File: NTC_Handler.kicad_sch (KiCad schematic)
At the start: 48 parts, among them U11 LMV7239M5/NOPB, U2 LM1117GS-5.0, U3 LM1117GS-5.0, U4 LMV7239M5/NOPB, U5 ADuM1200AR, U6 ADuM1200AR, U7 LM1117GS-5.0, U8 LMV7239M5/NOPB, U9 ADuM1200AR

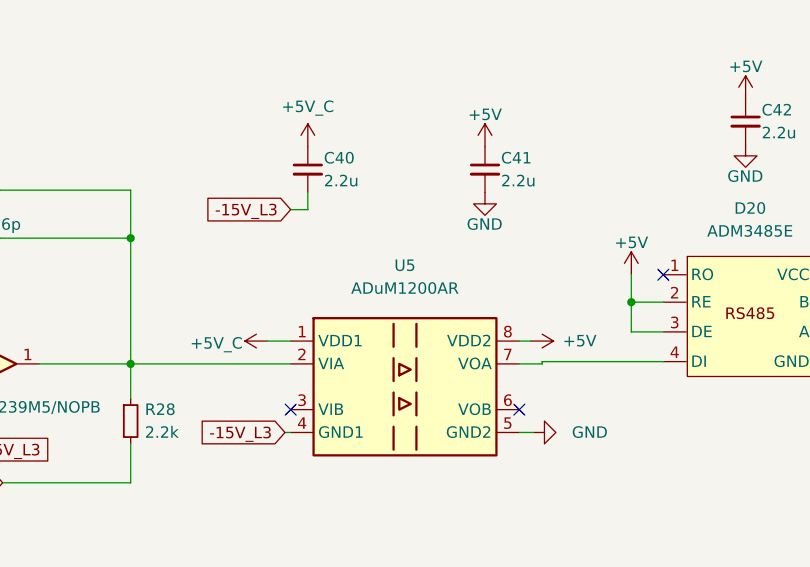
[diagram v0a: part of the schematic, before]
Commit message: Отправил на проверку в резонит: изменил BOM
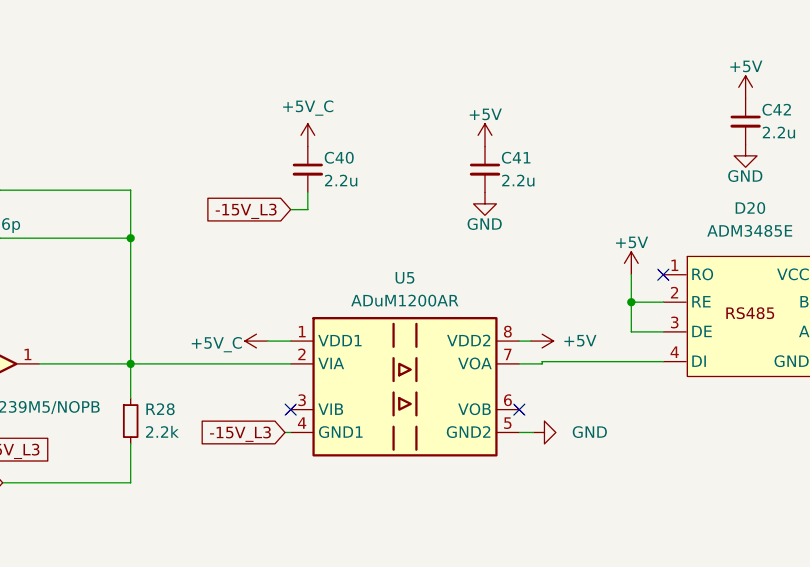
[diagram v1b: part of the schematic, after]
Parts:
- U5, U6, U9: Аналог (none) -> SCM3728ASA
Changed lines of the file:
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@@
 			)
 		)
+		(property "Аналог" "SCM3728ASA"
+			(at 212.725 152.4 0)
+			(effects
+				(font
+					(size 1.27 1.27)
+				)
+				(hide yes)
+			)
+		)
 		(pin "1"
 		)
@@
 			)
 		)
+		(property "Аналог" "SCM3728ASA"
+			(at 212.725 229.235 0)
+			(effects
+				(font
+					(size 1.27 1.27)
+				)
+				(hide yes)
+			)
+		)
 		(pin "1"
 		)
@@
 		(fields_autoplaced yes)
 		(property "Reference" "U5"
-			(at 212.725 63.373 0)
+			(at 212.725 64.77 0)
 			(effects
 				(font
@@
 		)
 		(property "Value" "ADuM1200AR"
-			(at 212.725 65.913 0)
+			(at 212.725 67.31 0)
 			(effects
 				(font
@@
 			(at 212.725 76.835 0)
 			(effects
+				(font
+					(size 1.27 1.27)
+				)
+				(hide yes)
+			)
+		)
+		(property "Аналог" "SCM3728ASA"
+			(at 212.725 76.835 0)
+			(effects

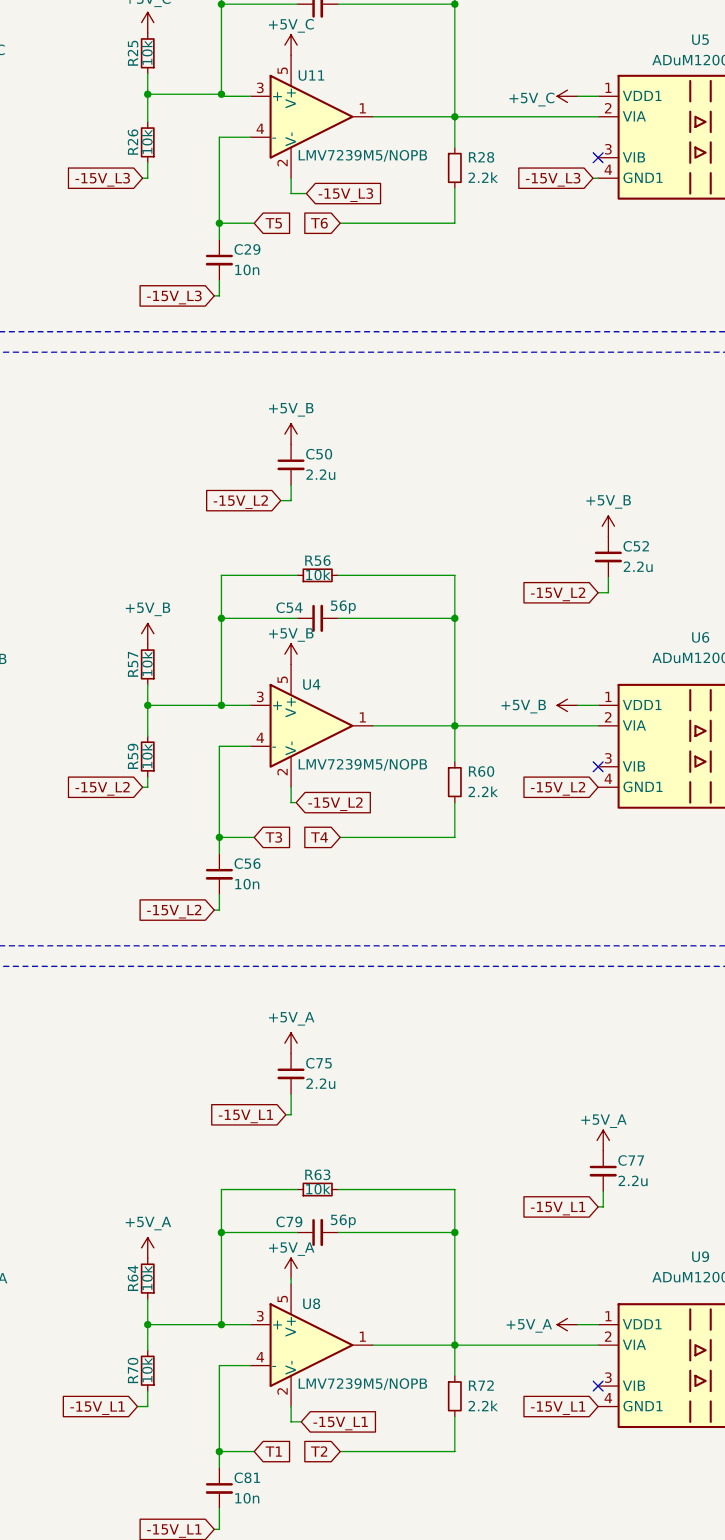
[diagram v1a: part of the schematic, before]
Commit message: Изменения: обновил BOM и названия в схеме
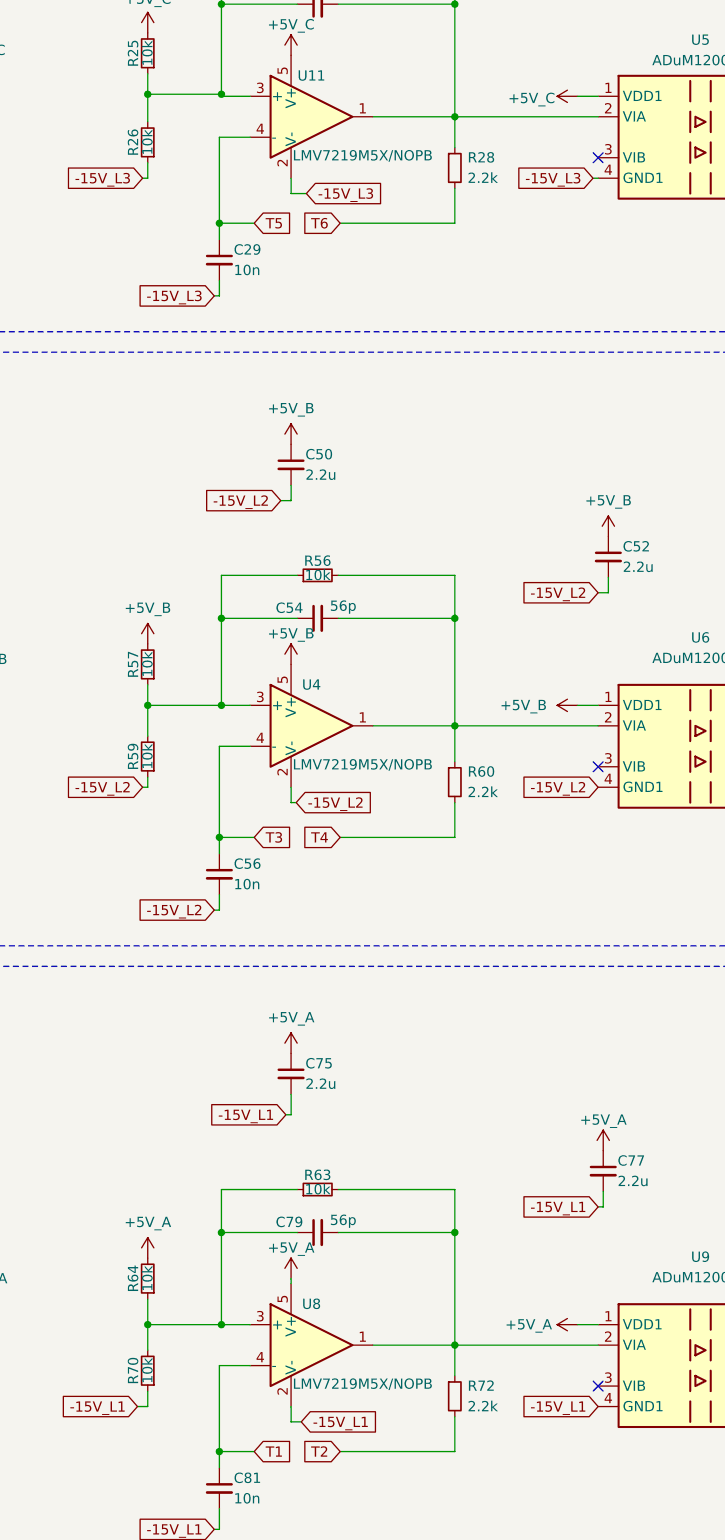
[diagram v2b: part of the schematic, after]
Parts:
- U11, U4, U8: value LMV7239M5/NOPB -> LMV7219M5X/NOPB
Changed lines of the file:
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@@
 			)
 		)
-		(property "Value" "LMV7239M5/NOPB"
+		(property "Value" "LMV7219M5X/NOPB"
 			(at 170.815 154.686 0)
 			(effects
@@
 			)
 		)
-		(property "Value" "LMV7239M5/NOPB"
+		(property "Value" "LMV7219M5X/NOPB"
 			(at 170.815 231.521 0)
 			(effects
@@
 			)
 		)
-		(property "Value" "LMV7239M5/NOPB"
+		(property "Value" "LMV7219M5X/NOPB"
 			(at 170.815 79.121 0)
 			(effects

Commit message: VER2.0: отпаравил файлы в китай, обновил BOM
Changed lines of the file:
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@@
 		)
 		(property "Value" "LMV7219M5X/NOPB"
-			(at 170.815 154.686 0)
+			(at 171.45 154.94 0)
 			(effects
 				(font
@@
 		)
 		(property "Value" "LMV7219M5X/NOPB"
-			(at 170.815 231.521 0)
+			(at 171.45 231.775 0)
 			(effects
 				(font
@@
 		)
 		(property "Value" "LMV7219M5X/NOPB"
-			(at 170.815 79.121 0)
+			(at 171.45 79.375 0)
 			(effects
 				(font

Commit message: VER2.2: все изменения в списке изменений
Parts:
- D20, D21, D22: value ADM3485E -> ~; Description P/N (none) -> RS485; Product Name (none) -> SN65HVD3082EDR
- U11, U4, U8: value LMV7219M5X/NOPB -> ~; Description P/N (none) -> Comparator; Product Name (none) -> LMV7219M5X/NOPB
- U2, U3, U7: value LM1117GS-5.0 -> ~; Description P/N (none) -> Linear regulator; Product Name (none) -> LM1117GS-5.0
- U5, U6, U9: value ADuM1200AR -> ~; Description P/N (none) -> Digital Isolator; Product Name (none) -> SCM3728ASA; Replacement (none) -> ADuM1200AR; Аналог SCM3728ASA -> (none)

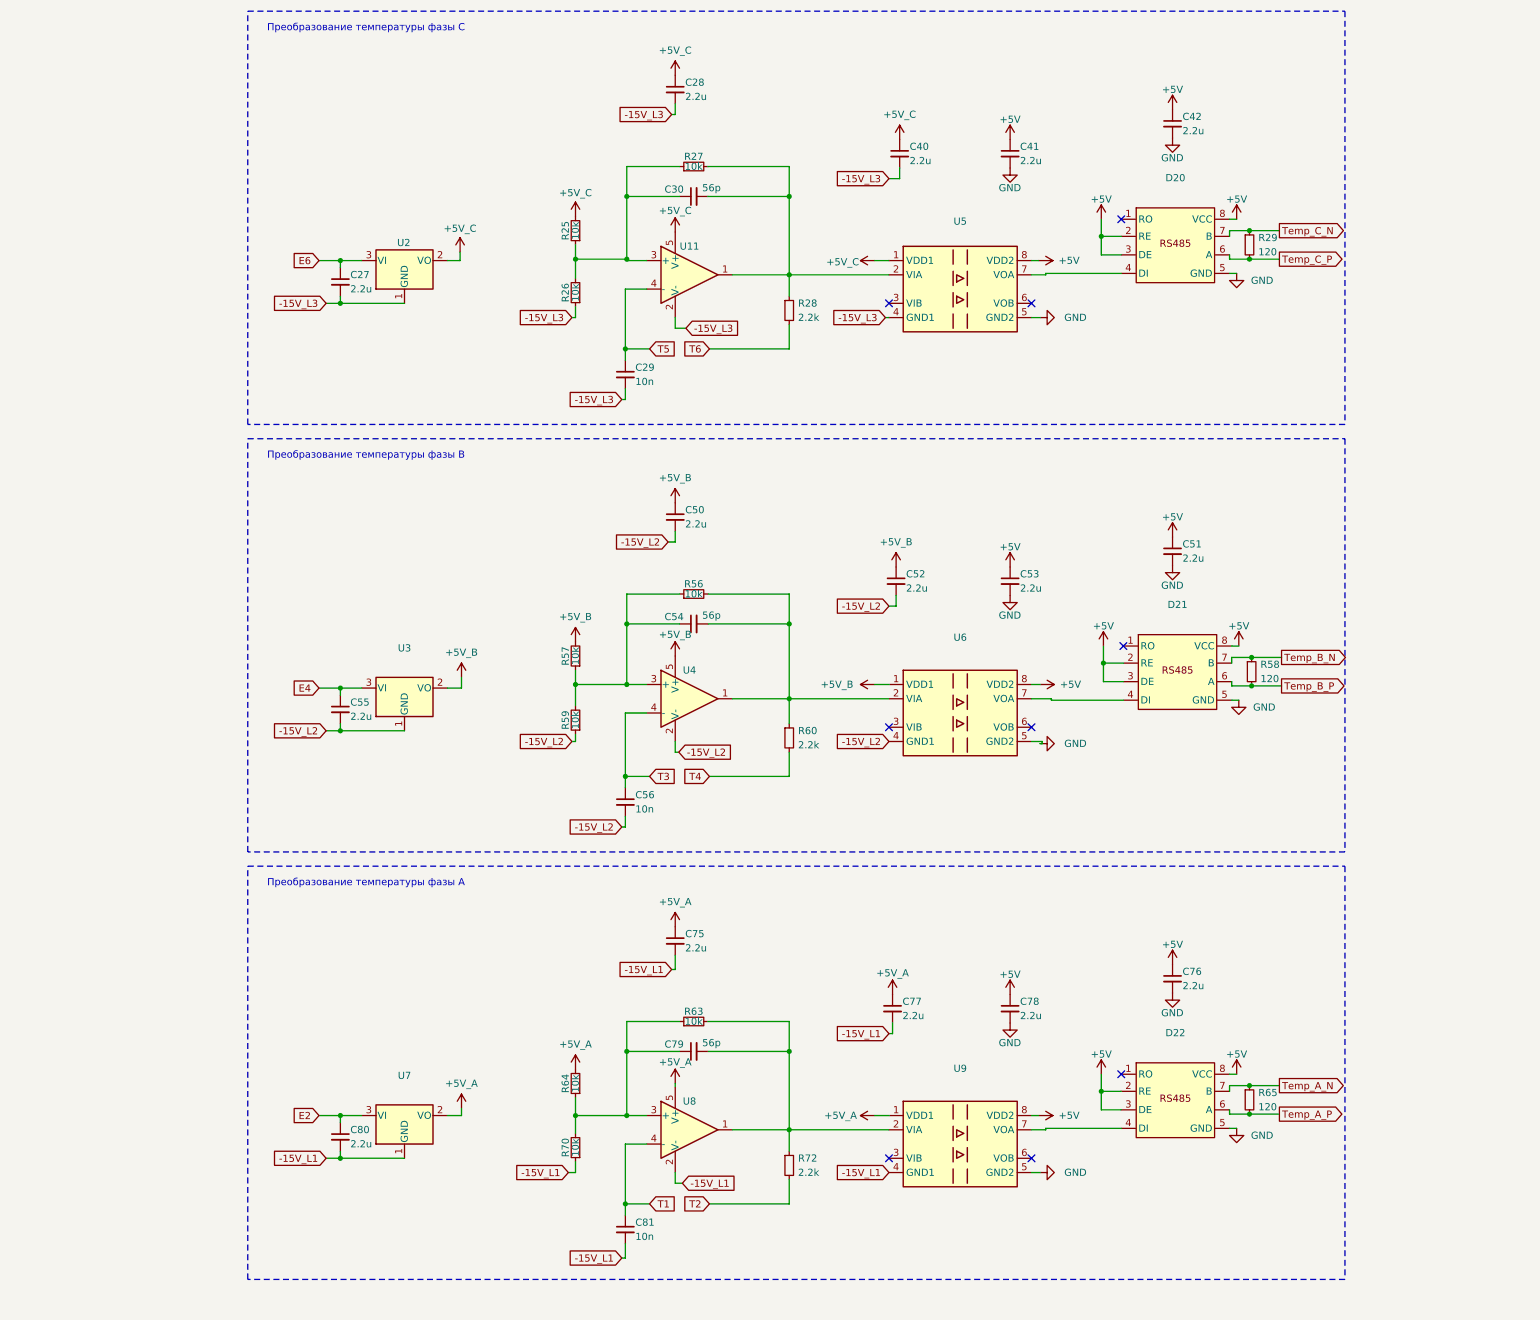
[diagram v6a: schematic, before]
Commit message: VER2.2: добавил фильтры на вход ШИМа и обновил все доки
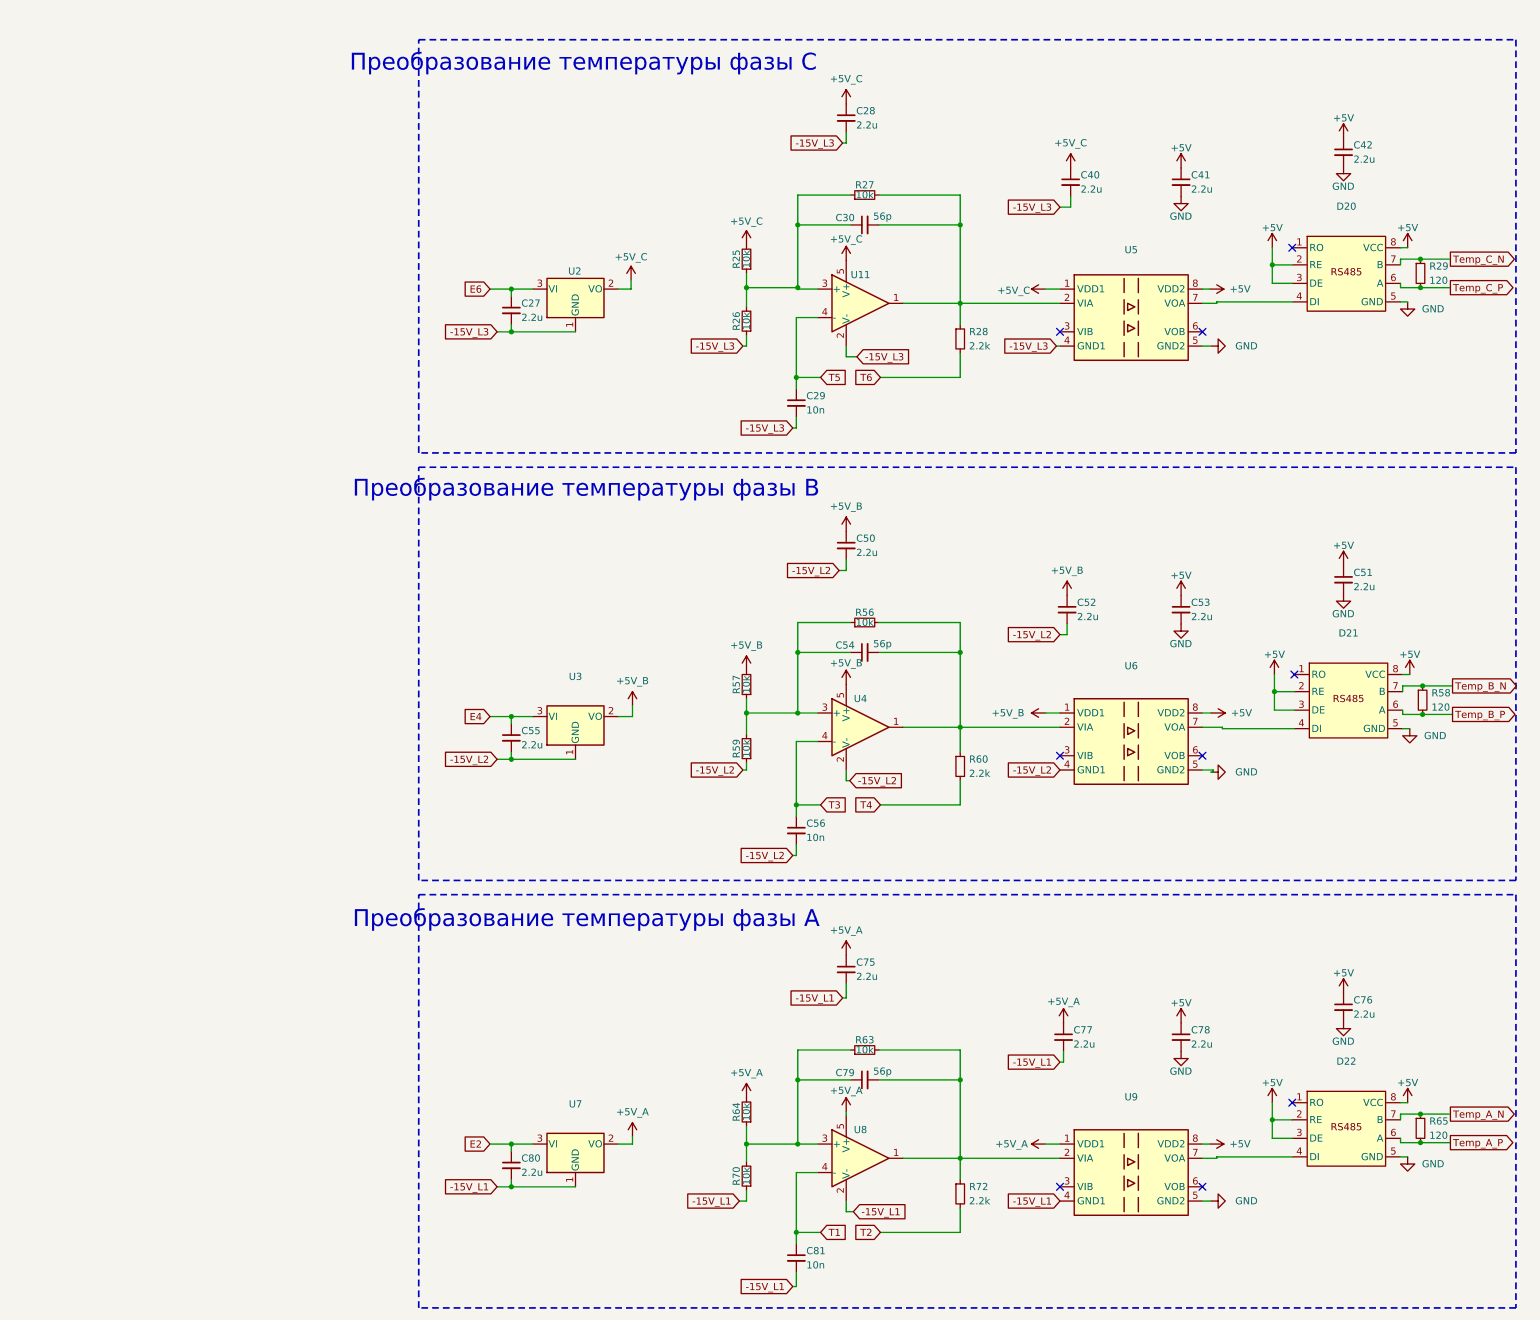
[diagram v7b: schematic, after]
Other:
- company: (none) -> ООО "ЭТТ"
- moved on the sheet: C27, C28, C29, C30, C40, C41, C42, C50, C51, C52, C53, C54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
